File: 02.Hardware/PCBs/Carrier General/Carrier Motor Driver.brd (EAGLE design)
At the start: 126 x 93 mm, 87 parts, among them IC1 MCP6001T-I_LT, IC2 AP62200WU-7, IC3 PCF8575DB, U1 MCP6002T-I/SN, U2 LM4040BIM3-2.0/NOPB, U3 ATE1D-5M3-10-Z

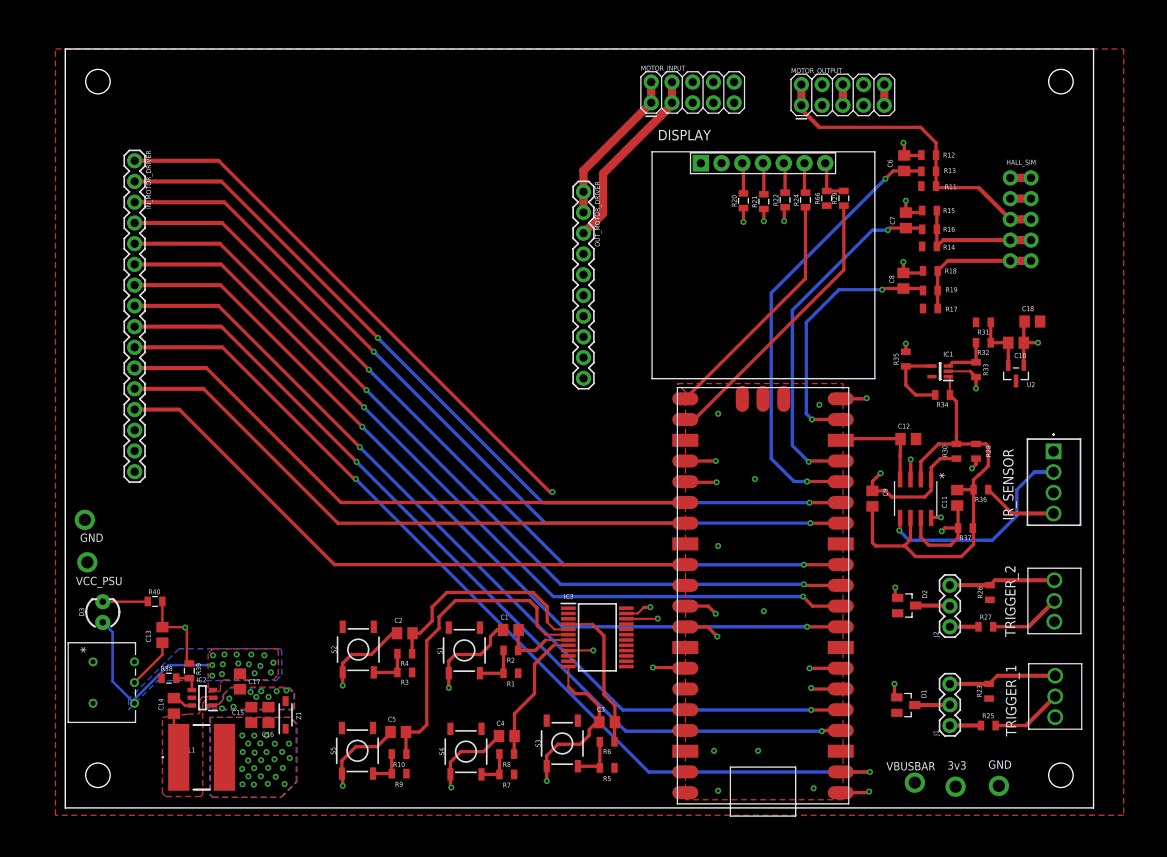
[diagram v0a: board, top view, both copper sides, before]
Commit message: Se añade 3v3 para filtro ISENSE + Cambios menores
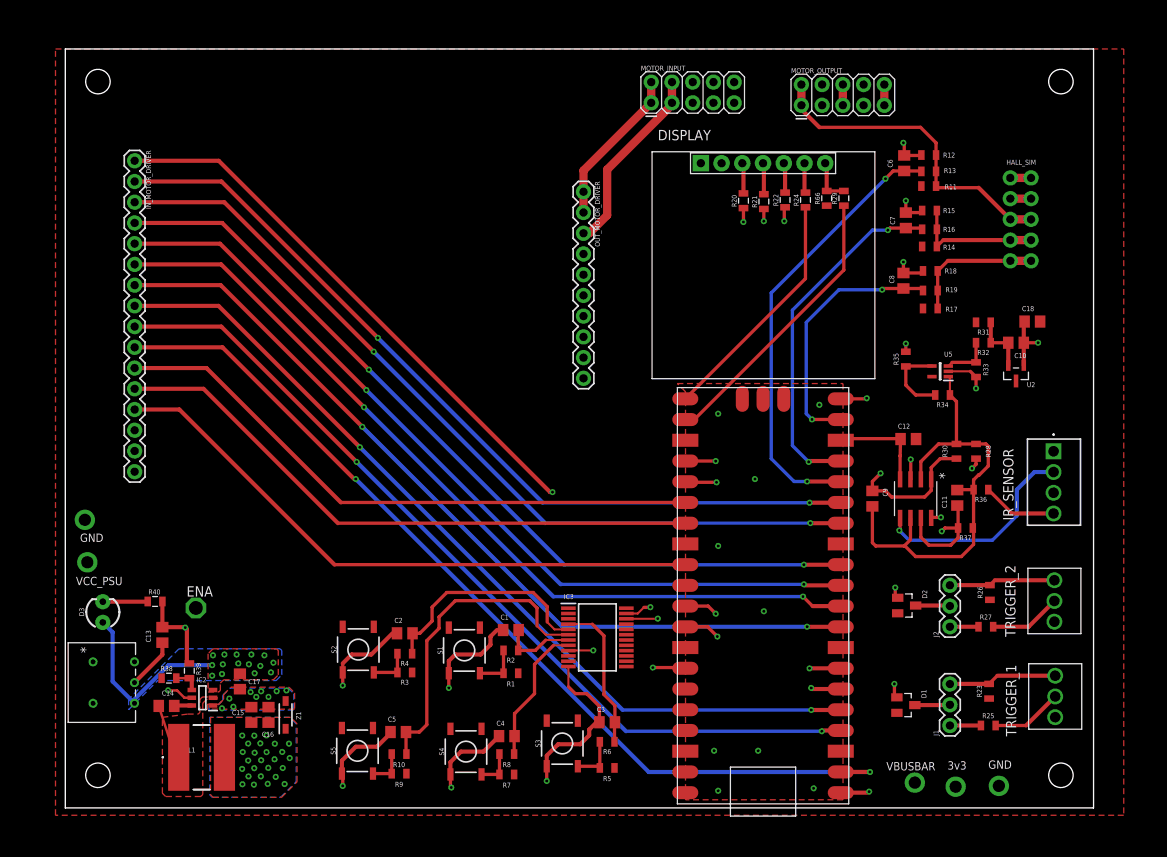
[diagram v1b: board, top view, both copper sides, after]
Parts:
- added ENA: TESTPAD_TPSQPAD1-17, BeagleBone_Blue_R3:TESTPAD_P1-17
- moved C14 0.90 mm to (12.4, 12.5), turned to 0 degrees
- renumbered IC1 to U5, U$1 to U4
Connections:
- net EN_DCDC: now also ENA.TP
- net GND: now also IC3.2, IC3.21, IC3.3; no longer OUT_MOTOR_DRIVER.10
- net VCC: now also OUT_MOTOR_DRIVER.10
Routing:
- net EN_DCDC: track 0.00 -> 15.2 mm, vias 0 -> 1
- net GND: track 134.5 -> 131.9 mm
- net N$32: track 5.60 -> 6.84 mm
- net T2: track 41.5 -> 42.7 mm

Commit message: Se pasa de 4 capas a 2 capas
El precio del prototipo es casi el doble con 4 caps
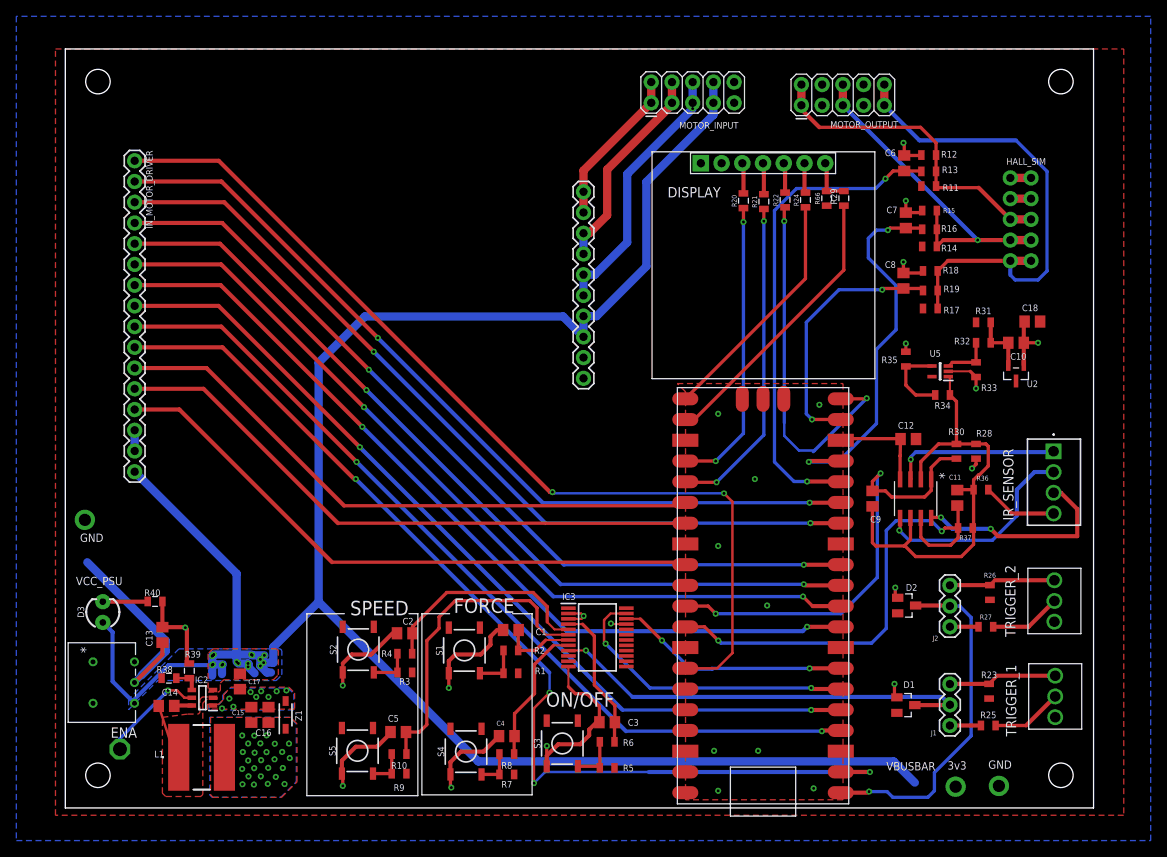
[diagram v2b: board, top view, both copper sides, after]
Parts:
- moved ENA 19.6 mm to (6.70, 7.20)
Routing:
- net VBUSBAR: track 247.0 -> 267.2 mm, vias 16 -> 17
- net ISENSE: track 99.0 -> 115.8 mm
- net DSP_RST: track 30.8 -> 45.0 mm
- net EN_5: track 115.2 -> 127.0 mm, vias 2 -> 4
- net VCC: track 18.8 -> 28.5 mm, vias 28 -> 29
- net GND: track 131.9 -> 138.6 mm, vias 34 -> 36
- net SENSOR_A: track 54.6 -> 60.0 mm
- net SENSOR_2: track 54.8 -> 59.9 mm
- net SENSOR_1: track 50.6 -> 55.4 mm
- net SDA: track 32.5 -> 37.2 mm
- net SENSOR_B: track 43.5 -> 46.5 mm
- net HALL_C: track 64.5 -> 61.5 mm
- net EN_DCDC: track 15.2 -> 12.9 mm
- net MOTOR_C: track 31.7 -> 32.5 mm, vias 0 -> 1
- net ON/OFF: track 18.5 -> 17.8 mm
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- removed copper zone on layer 15, net GND
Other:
- board text added: "<<"
- board text added: ">>"
- board text added: "FORCE"
- board text added: "ON/OFF"
- board text added: "SPEED"

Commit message: ERC Pasado. Cambios menores
Al pasar el ERC se detecta fallo en la alimentacion del  pull-up de la linea de CS de la pantalla. Se soluciona cambiando a la alimentacion de 3v3.
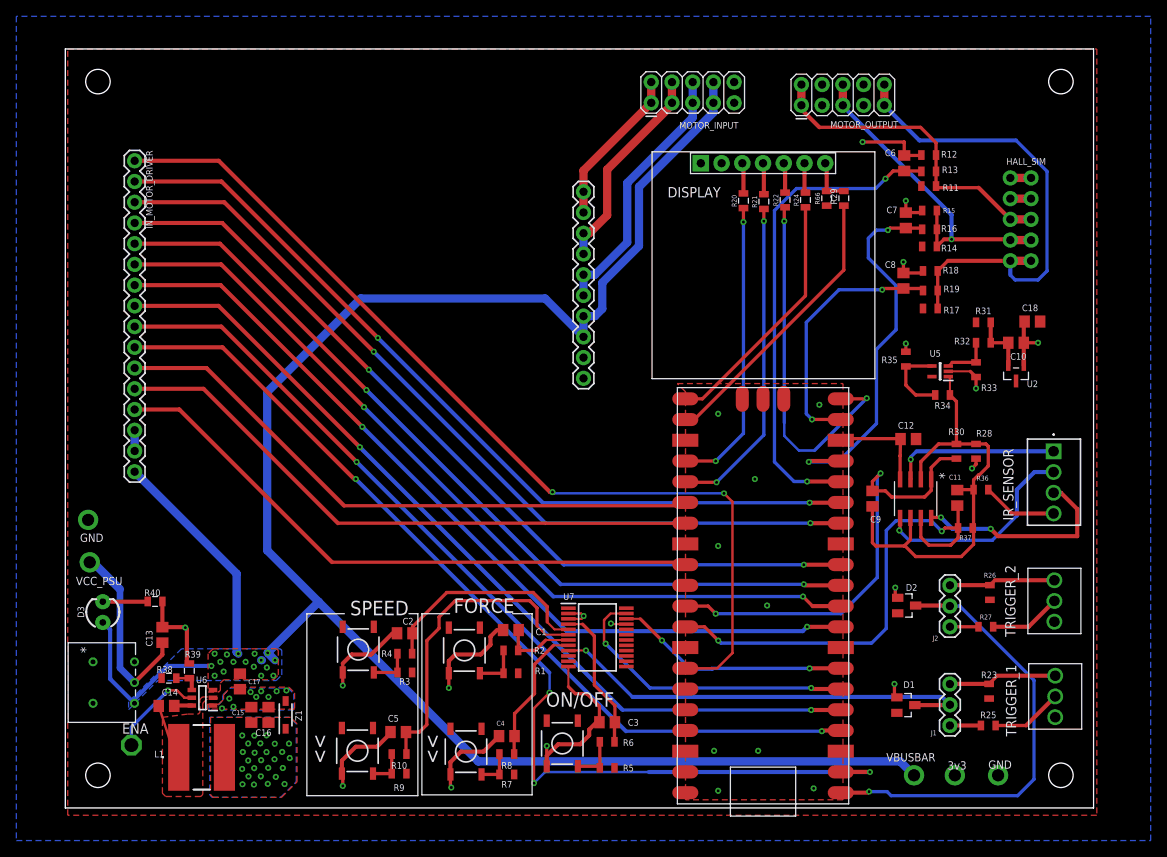
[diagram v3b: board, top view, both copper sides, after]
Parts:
- moved ENA 1.49 mm to (8.10, 7.70)
- renumbered IC2 to U6, IC3 to U7
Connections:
- removed net N$27: U7.10
- removed net N$29: U7.11
- removed net VCC-ISO: R66.1
- net VCC: now also R66.1
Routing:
- net T2: track 42.7 -> 55.2 mm
- net VBUSBAR: track 267.2 -> 255.0 mm, vias 17 -> 18
- net HALL_B: track 46.2 -> 40.8 mm
- net GND: track 138.6 -> 143.8 mm
- net VCC_PSU: track 26.6 -> 23.6 mm, vias 0 -> 1
- net MISO: track 29.6 -> 30.8 mm
- net EN_DCDC: track 12.9 -> 11.8 mm
- net IN_SENSOR_1: vias 2 -> 1
- net MOTOR_C: vias 1 -> 0

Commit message: Cambios antes de Produccion
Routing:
- net SENSOR_B: track 46.5 -> 43.7 mm
- net VBUSBAR: track 255.0 -> 252.9 mm
- net SENSOR_2: track 59.9 -> 58.4 mm
- net VCC: track 28.5 -> 27.9 mm
